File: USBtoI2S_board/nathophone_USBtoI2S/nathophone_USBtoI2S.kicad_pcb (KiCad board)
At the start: 4 copper layers, 80 x 40 mm, 105 parts, among them J1 UJ20-C-H-G-SMT-5-P16-TR, J2 FTSH-110-01-F-DV-K, J3 Conn_01x30, J4 FTSH-105-01-F-DV-P-TR, Q1 MMBT3904, SW1 PEC09-2320F-S0015, U1 IS25LP032D-JKLE, U2 XU316-1024-TQ128-C24, U3 TPS62410DRCR, U4 MAX809STRG, U5 74LVC2G07, Y1 FA-238 24MHz

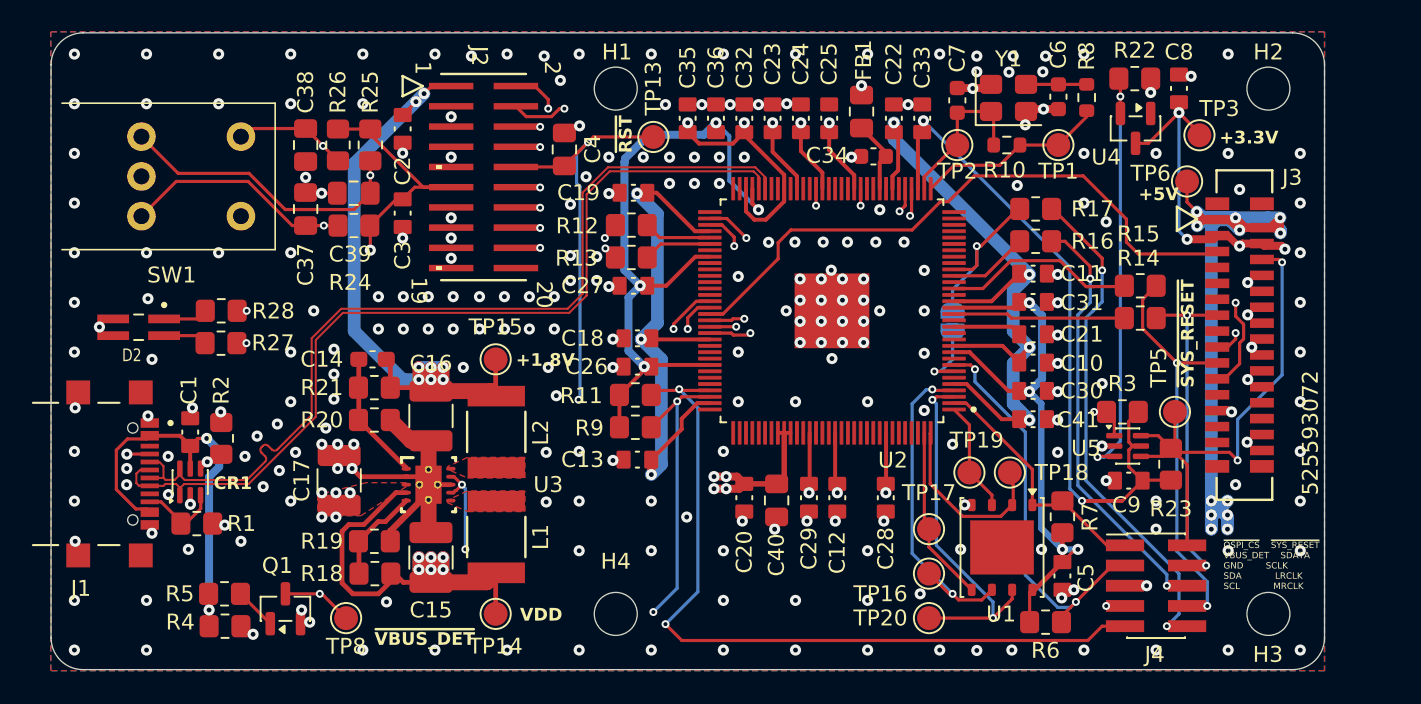
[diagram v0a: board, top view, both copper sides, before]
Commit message: ADDED USBtoI2S board design files
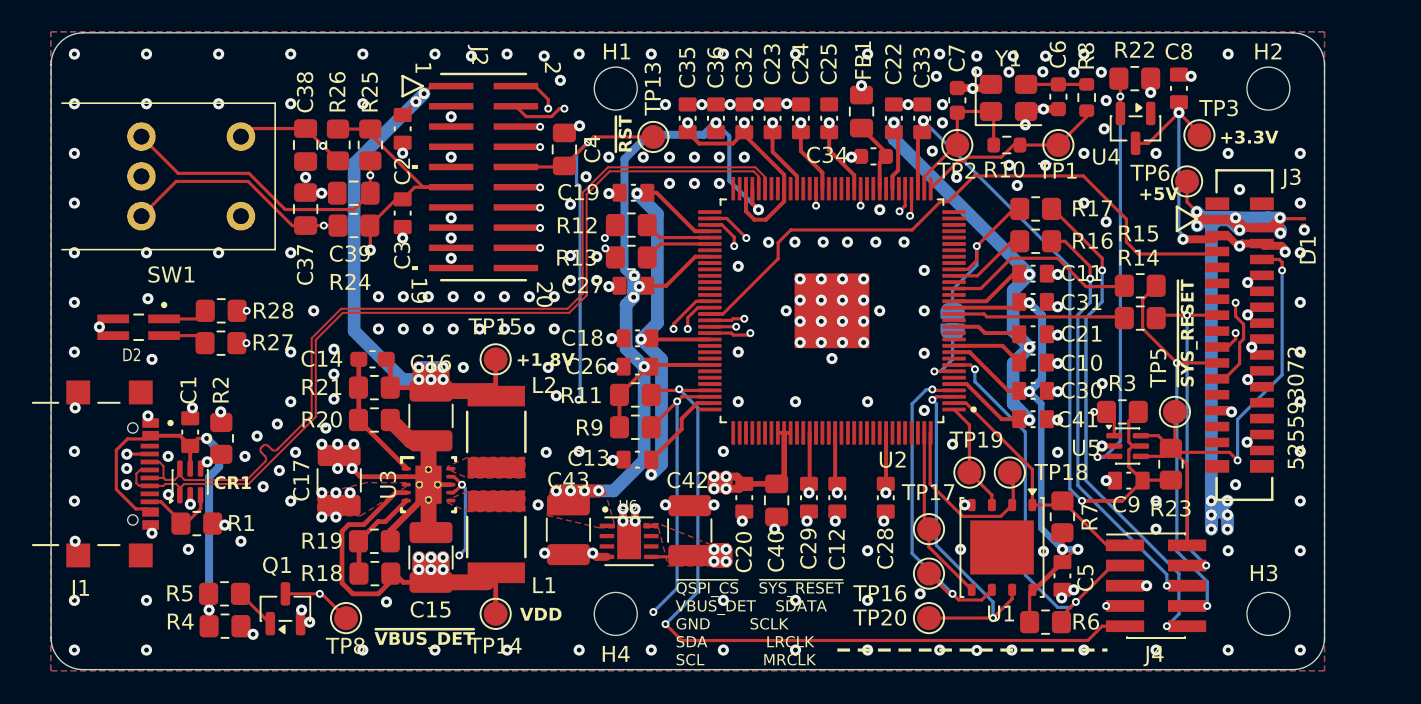
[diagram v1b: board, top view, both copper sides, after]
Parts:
- added C42: 10u, Capacitor_SMD:C_1210_3225Metric_Pad1.33x2.70mm_HandSolder, F.Cu at (158.0, 101.4)
- added C43: 10u, Capacitor_SMD:C_1210_3225Metric_Pad1.33x2.70mm_HandSolder, F.Cu at (150.4, 101.4)
- added D1: 5.6V, USB_to_I2S_Board:SOD-962_SL2_TOS, F.Cu at (196.5, 82.0)
- added U6: AP7361C-33FGE-7, USB_to_I2S_Board:SON65P300X300X63-9N, F.Cu at (154.2, 102.1)
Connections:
- U1 pad 9: GND -> (no net)
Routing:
- net +3.3V: track 202.7 -> 219.6 mm, vias 15 -> 21
- net +5V: track 128.2 -> 141.3 mm, vias 17 -> 21
- net GND: track 27.2 -> 29.7 mm, vias 258 -> 271
- net VDD: track 197.6 -> 200.0 mm
- net /Power/~{3.3V_RESET}: track 75.0 -> 76.1 mm
- net Rot_Enc_SW: track 47.1 -> 47.7 mm
- added copper zone on F.Cu, net +3.3V
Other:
- board text added: "MCLK_X0D11-X1D11"
